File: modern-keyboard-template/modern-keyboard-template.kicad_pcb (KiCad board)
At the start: 2 copper layers, 44 x 44.1 mm, 25 parts, among them J1 USB_C_Receptacle_USB2.0, J2 Conn_01x05, U1 STM32F072CBT6, U2 PRTR5V0U2X, U3 XC6206PxxxMR-Regulator_Linear, U5 TXB0101

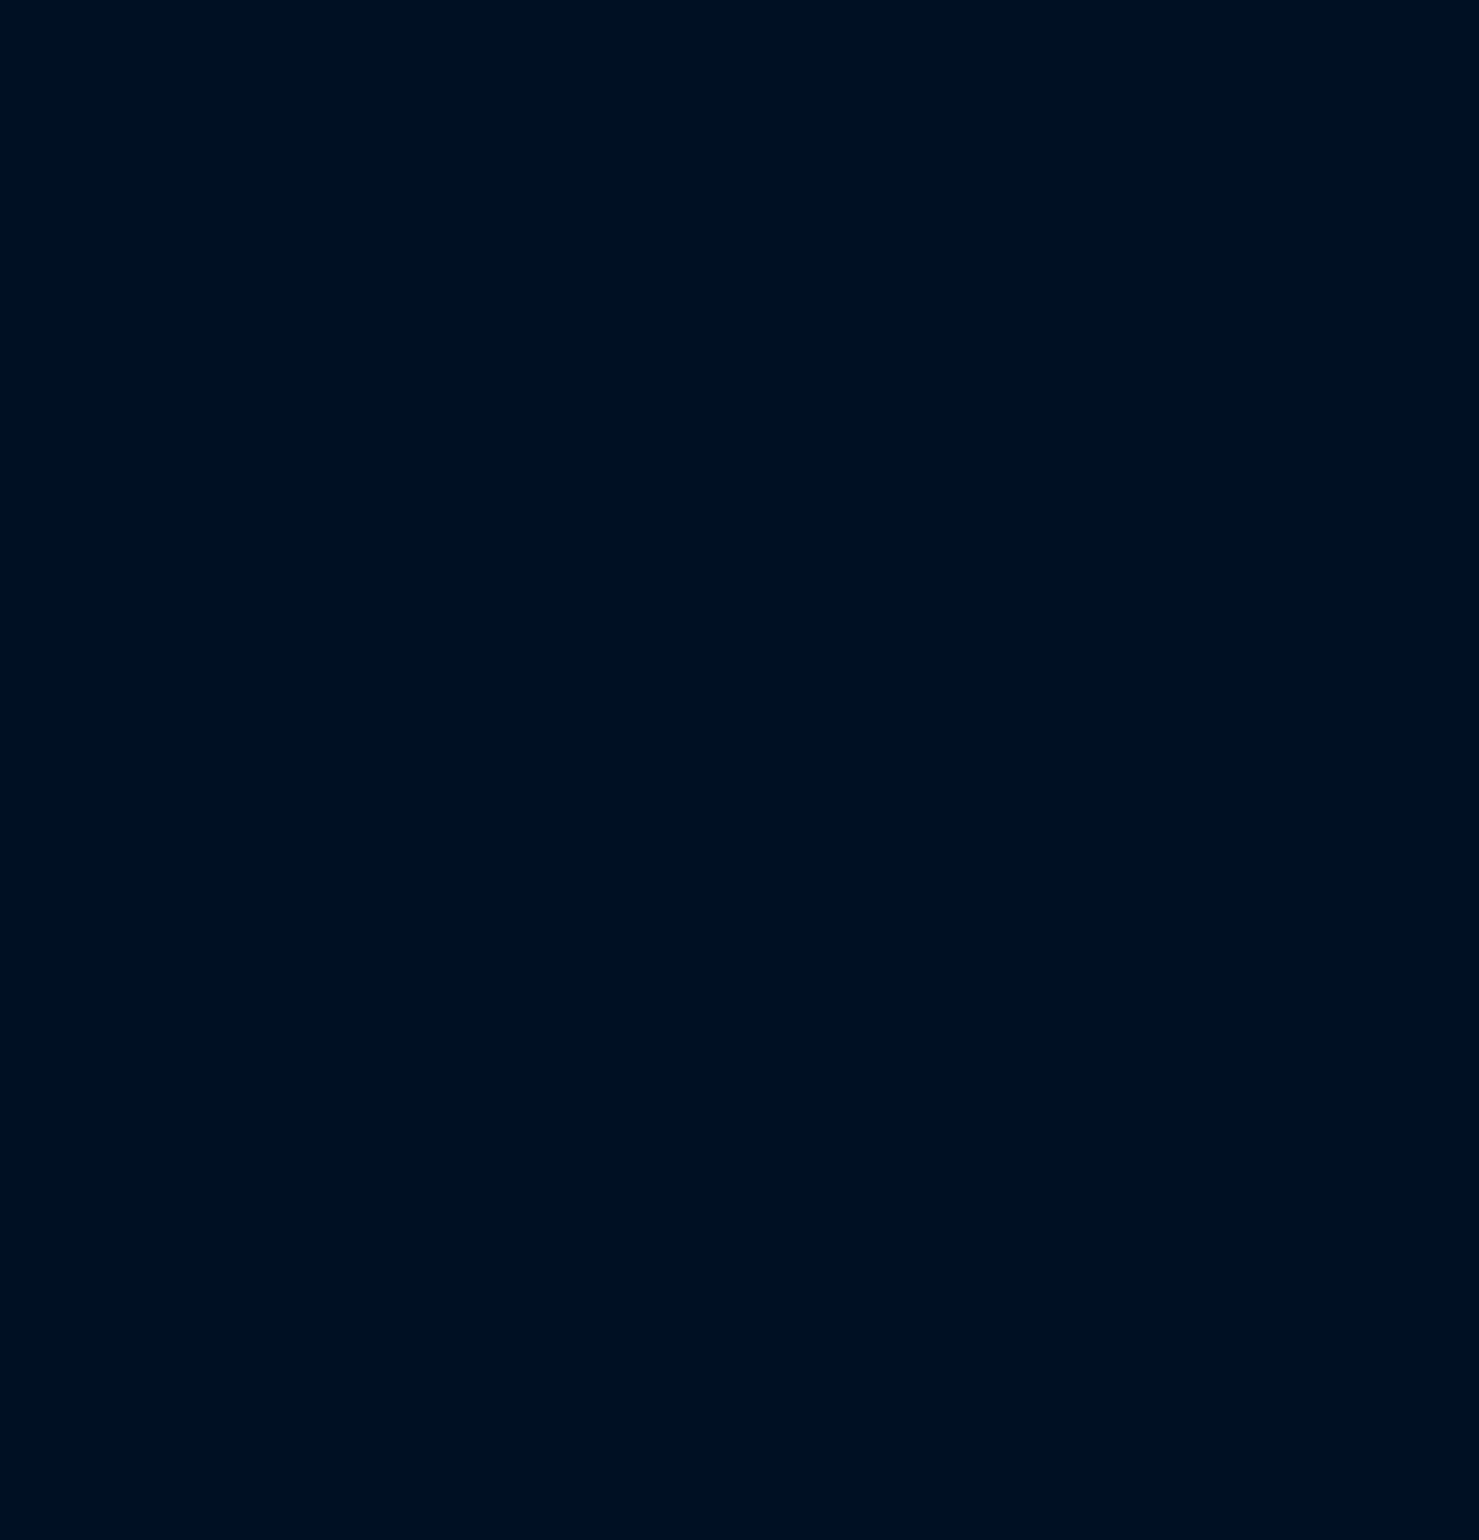
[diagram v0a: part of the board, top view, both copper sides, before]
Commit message: updated pcb w/ switches
need to revisit this entire design tbh
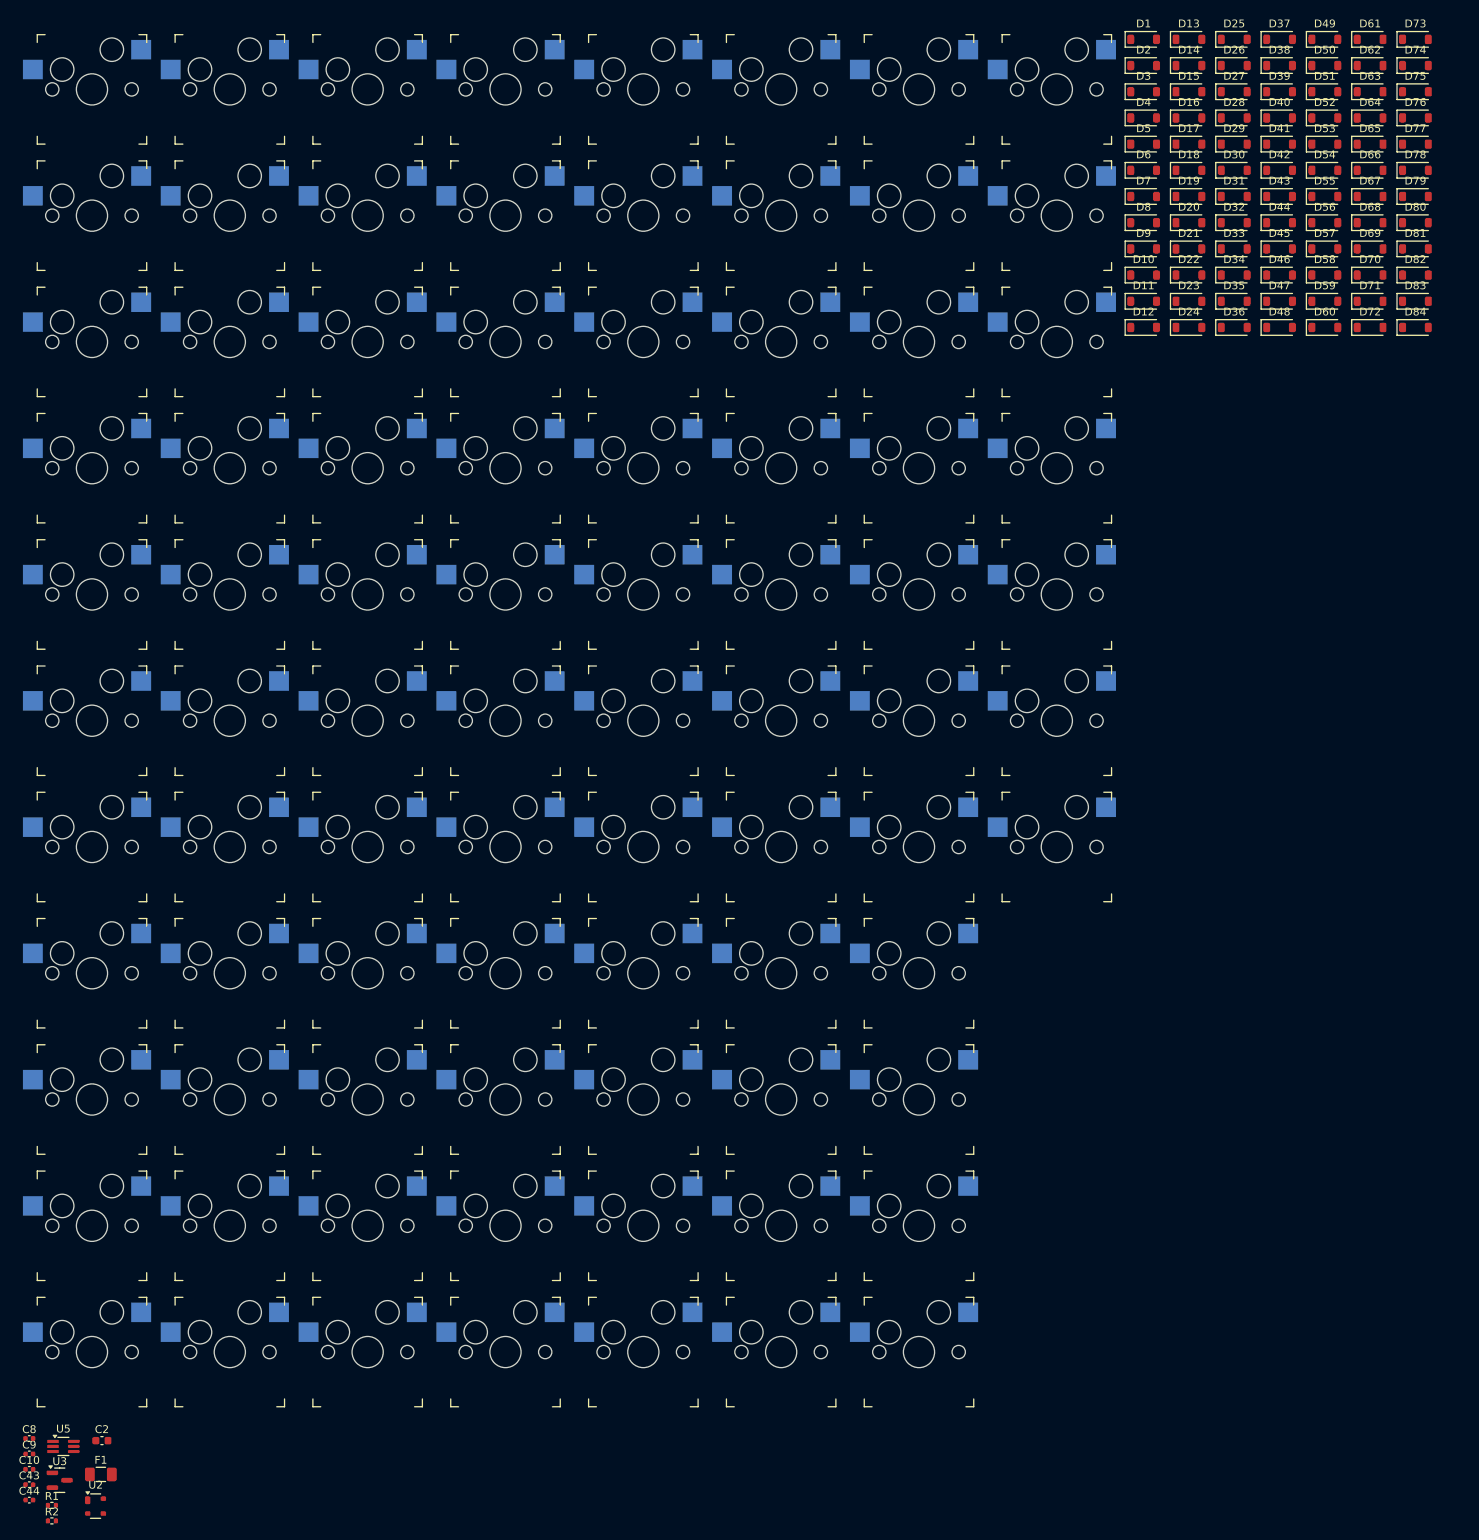
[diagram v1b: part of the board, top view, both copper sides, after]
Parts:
- added C10: 1uF, Capacitor_SMD:C_0402_1005Metric, F.Cu at (-32.3, 108.8)
- added C2: 10uF, Capacitor_SMD:C_0603_1608Metric, F.Cu at (-23.0, 105.2)
- added C43: 0.1uF, Capacitor_SMD:C_0402_1005Metric, F.Cu at (-32.3, 110.8)
- added C44: 0.1uF, Capacitor_SMD:C_0402_1005Metric, F.Cu at (-32.3, 112.8)
- added C8: 100nF, Capacitor_SMD:C_0402_1005Metric, F.Cu at (-32.3, 104.9)
- added C9: 1uF, Capacitor_SMD:C_0402_1005Metric, F.Cu at (-32.3, 106.9)
- added D1: D, Diode_SMD:D_SOD-123, F.Cu at (110.3, -74.1)
- added D10: D, Diode_SMD:D_SOD-123, F.Cu at (110.3, -43.9)
- added D11: D, Diode_SMD:D_SOD-123, F.Cu at (110.3, -40.6)
- added D12: D, Diode_SMD:D_SOD-123, F.Cu at (110.3, -37.2)
- added D13: D, Diode_SMD:D_SOD-123, F.Cu at (116.1, -74.1)
- added D14: D, Diode_SMD:D_SOD-123, F.Cu at (116.1, -70.7)
- added D15: D, Diode_SMD:D_SOD-123, F.Cu at (116.1, -67.4)
- added D16: D, Diode_SMD:D_SOD-123, F.Cu at (116.1, -64.0)
- added D17: D, Diode_SMD:D_SOD-123, F.Cu at (116.1, -60.7)
- added D18: D, Diode_SMD:D_SOD-123, F.Cu at (116.1, -57.3)
- added D19: D, Diode_SMD:D_SOD-123, F.Cu at (116.1, -54.0)
- added D2: D, Diode_SMD:D_SOD-123, F.Cu at (110.3, -70.7)
- added D20: D, Diode_SMD:D_SOD-123, F.Cu at (116.1, -50.6)
- added D21: D, Diode_SMD:D_SOD-123, F.Cu at (116.1, -47.3)
- added D22: D, Diode_SMD:D_SOD-123, F.Cu at (116.1, -43.9)
- added D23: D, Diode_SMD:D_SOD-123, F.Cu at (116.1, -40.6)
- added D24: D, Diode_SMD:D_SOD-123, F.Cu at (116.1, -37.2)
- added D25: D, Diode_SMD:D_SOD-123, F.Cu at (121.9, -74.1)
- added D26: D, Diode_SMD:D_SOD-123, F.Cu at (121.9, -70.7)
- added D27: D, Diode_SMD:D_SOD-123, F.Cu at (121.9, -67.4)
- added D28: D, Diode_SMD:D_SOD-123, F.Cu at (121.9, -64.0)
- added D29: D, Diode_SMD:D_SOD-123, F.Cu at (121.9, -60.7)
- added D3: D, Diode_SMD:D_SOD-123, F.Cu at (110.3, -67.4)
- added D30: D, Diode_SMD:D_SOD-123, F.Cu at (121.9, -57.3)
- added D31: D, Diode_SMD:D_SOD-123, F.Cu at (121.9, -54.0)
- added D32: D, Diode_SMD:D_SOD-123, F.Cu at (121.9, -50.6)
- added D33: D, Diode_SMD:D_SOD-123, F.Cu at (121.9, -47.3)
- added D34: D, Diode_SMD:D_SOD-123, F.Cu at (121.9, -43.9)
- added D35: D, Diode_SMD:D_SOD-123, F.Cu at (121.9, -40.6)
- added D36: D, Diode_SMD:D_SOD-123, F.Cu at (121.9, -37.2)
- added D37: D, Diode_SMD:D_SOD-123, F.Cu at (127.7, -74.1)
- added D38: D, Diode_SMD:D_SOD-123, F.Cu at (127.7, -70.7)
- added D39: D, Diode_SMD:D_SOD-123, F.Cu at (127.7, -67.4)
- added D4: D, Diode_SMD:D_SOD-123, F.Cu at (110.3, -64.0)
- added D40: D, Diode_SMD:D_SOD-123, F.Cu at (127.7, -64.0)
- added D41: D, Diode_SMD:D_SOD-123, F.Cu at (127.7, -60.7)
- added D42: D, Diode_SMD:D_SOD-123, F.Cu at (127.7, -57.3)
- added D43: D, Diode_SMD:D_SOD-123, F.Cu at (127.7, -54.0)
- added D44: D, Diode_SMD:D_SOD-123, F.Cu at (127.7, -50.6)
- added D45: D, Diode_SMD:D_SOD-123, F.Cu at (127.7, -47.3)
- added D46: D, Diode_SMD:D_SOD-123, F.Cu at (127.7, -43.9)
- added D47: D, Diode_SMD:D_SOD-123, F.Cu at (127.7, -40.6)
- added D48: D, Diode_SMD:D_SOD-123, F.Cu at (127.7, -37.2)
- added D49: D, Diode_SMD:D_SOD-123, F.Cu at (133.4, -74.1)
- added D5: D, Diode_SMD:D_SOD-123, F.Cu at (110.3, -60.7)
- added D50: D, Diode_SMD:D_SOD-123, F.Cu at (133.4, -70.7)
- added D51: D, Diode_SMD:D_SOD-123, F.Cu at (133.4, -67.4)
- added D52: D, Diode_SMD:D_SOD-123, F.Cu at (133.4, -64.0)
- added D53: D, Diode_SMD:D_SOD-123, F.Cu at (133.4, -60.7)
- added D54: D, Diode_SMD:D_SOD-123, F.Cu at (133.4, -57.3)
- added D55: D, Diode_SMD:D_SOD-123, F.Cu at (133.4, -54.0)
- added D56: D, Diode_SMD:D_SOD-123, F.Cu at (133.4, -50.6)
- added D57: D, Diode_SMD:D_SOD-123, F.Cu at (133.4, -47.3)
- added D58: D, Diode_SMD:D_SOD-123, F.Cu at (133.4, -43.9)
- added D59: D, Diode_SMD:D_SOD-123, F.Cu at (133.4, -40.6)
- added D6: D, Diode_SMD:D_SOD-123, F.Cu at (110.3, -57.3)
- added D60: D, Diode_SMD:D_SOD-123, F.Cu at (133.4, -37.2)
- added D61: D, Diode_SMD:D_SOD-123, F.Cu at (139.2, -74.1)
- added D62: D, Diode_SMD:D_SOD-123, F.Cu at (139.2, -70.7)
- added D63: D, Diode_SMD:D_SOD-123, F.Cu at (139.2, -67.4)
- added D64: D, Diode_SMD:D_SOD-123, F.Cu at (139.2, -64.0)
- added D65: D, Diode_SMD:D_SOD-123, F.Cu at (139.2, -60.7)
- added D66: D, Diode_SMD:D_SOD-123, F.Cu at (139.2, -57.3)
- added D67: D, Diode_SMD:D_SOD-123, F.Cu at (139.2, -54.0)
- added D68: D, Diode_SMD:D_SOD-123, F.Cu at (139.2, -50.6)
- added D69: D, Diode_SMD:D_SOD-123, F.Cu at (139.2, -47.3)
- added D7: D, Diode_SMD:D_SOD-123, F.Cu at (110.3, -54.0)
- added D70: D, Diode_SMD:D_SOD-123, F.Cu at (139.2, -43.9)
- added D71: D, Diode_SMD:D_SOD-123, F.Cu at (139.2, -40.6)
- added D72: D, Diode_SMD:D_SOD-123, F.Cu at (139.2, -37.2)
- added D73: D, Diode_SMD:D_SOD-123, F.Cu at (145.0, -74.1)
- added D74: D, Diode_SMD:D_SOD-123, F.Cu at (145.0, -70.7)
- added D75: D, Diode_SMD:D_SOD-123, F.Cu at (145.0, -67.4)
- added D76: D, Diode_SMD:D_SOD-123, F.Cu at (145.0, -64.0)
- added D77: D, Diode_SMD:D_SOD-123, F.Cu at (145.0, -60.7)
- added D78: D, Diode_SMD:D_SOD-123, F.Cu at (145.0, -57.3)
- added D79: D, Diode_SMD:D_SOD-123, F.Cu at (145.0, -54.0)
- added D8: D, Diode_SMD:D_SOD-123, F.Cu at (110.3, -50.6)
- added D80: D, Diode_SMD:D_SOD-123, F.Cu at (145.0, -50.6)
- added D81: D, Diode_SMD:D_SOD-123, F.Cu at (145.0, -47.3)
- added D82: D, Diode_SMD:D_SOD-123, F.Cu at (145.0, -43.9)
- added D83: D, Diode_SMD:D_SOD-123, F.Cu at (145.0, -40.6)
- added D84: D, Diode_SMD:D_SOD-123, F.Cu at (145.0, -37.2)
- added D9: D, Diode_SMD:D_SOD-123, F.Cu at (110.3, -47.3)
- added F1: 500mA, Fuse:Fuse_1206_3216Metric, F.Cu at (-23.1, 109.5)
- added R1: 5.1k, Resistor_SMD:R_0402_1005Metric, F.Cu at (-29.4, 113.4)
- added R2: 5.1k, Resistor_SMD:R_0402_1005Metric, F.Cu at (-29.4, 115.4)
- added SW1: ~, switches:Kailh_socket_MX, F.Cu at (-24.2, -67.7)
- added SW10: ~, switches:Kailh_socket_MX, F.Cu at (-24.2, 77.7)
- added SW11: ~, switches:Kailh_socket_MX, F.Cu at (-24.2, 93.8)
- added SW12: ~, switches:Kailh_socket_MX, F.Cu at (-6.62, -67.7)
- added SW13: ~, switches:Kailh_socket_MX, F.Cu at (-6.62, -51.5)
- added SW14: ~, switches:Kailh_socket_MX, F.Cu at (-6.62, -35.4)
- added SW15: ~, switches:Kailh_socket_MX, F.Cu at (-6.62, -19.2)
- added SW16: ~, switches:Kailh_socket_MX, F.Cu at (-6.62, -3.06)
- added SW17: ~, switches:Kailh_socket_MX, F.Cu at (-6.62, 13.1)
- added SW18: ~, switches:Kailh_socket_MX, F.Cu at (-6.62, 29.2)
- added SW19: ~, switches:Kailh_socket_MX, F.Cu at (-6.62, 45.4)
- added SW2: ~, switches:Kailh_socket_MX, F.Cu at (-24.2, -51.5)
- added SW20: ~, switches:Kailh_socket_MX, F.Cu at (-6.62, 61.5)
- added SW21: ~, switches:Kailh_socket_MX, F.Cu at (-6.62, 77.7)
- added SW22: ~, switches:Kailh_socket_MX, F.Cu at (-6.62, 93.8)
- added SW23: ~, switches:Kailh_socket_MX, F.Cu at (11.0, -67.7)
- added SW24: ~, switches:Kailh_socket_MX, F.Cu at (11.0, -51.5)
- added SW25: ~, switches:Kailh_socket_MX, F.Cu at (11.0, -35.4)
- added SW26: ~, switches:Kailh_socket_MX, F.Cu at (11.0, -19.2)
- added SW27: ~, switches:Kailh_socket_MX, F.Cu at (11.0, -3.06)
- added SW28: ~, switches:Kailh_socket_MX, F.Cu at (11.0, 13.1)
- added SW29: ~, switches:Kailh_socket_MX, F.Cu at (11.0, 29.2)
- added SW3: ~, switches:Kailh_socket_MX, F.Cu at (-24.2, -35.4)
- added SW30: ~, switches:Kailh_socket_MX, F.Cu at (11.0, 45.4)
- added SW31: ~, switches:Kailh_socket_MX, F.Cu at (11.0, 61.5)
- added SW32: ~, switches:Kailh_socket_MX, F.Cu at (11.0, 77.7)
- added SW33: ~, switches:Kailh_socket_MX, F.Cu at (11.0, 93.8)
- added SW34: ~, switches:Kailh_socket_MX, F.Cu at (28.6, -67.7)
- added SW35: ~, switches:Kailh_socket_MX, F.Cu at (28.6, -51.5)
- added SW36: ~, switches:Kailh_socket_MX, F.Cu at (28.6, -35.4)
- added SW37: ~, switches:Kailh_socket_MX, F.Cu at (28.6, -19.2)
- added SW38: ~, switches:Kailh_socket_MX, F.Cu at (28.6, -3.06)
- added SW39: ~, switches:Kailh_socket_MX, F.Cu at (28.6, 13.1)
- added SW4: ~, switches:Kailh_socket_MX, F.Cu at (-24.2, -19.2)
- added SW40: ~, switches:Kailh_socket_MX, F.Cu at (28.6, 29.2)
- added SW41: ~, switches:Kailh_socket_MX, F.Cu at (28.6, 45.4)
- added SW42: ~, switches:Kailh_socket_MX, F.Cu at (28.6, 61.5)
- added SW43: ~, switches:Kailh_socket_MX, F.Cu at (28.6, 77.7)
- added SW44: ~, switches:Kailh_socket_MX, F.Cu at (28.6, 93.8)
- added SW45: ~, switches:Kailh_socket_MX, F.Cu at (46.3, -67.7)
- added SW46: ~, switches:Kailh_socket_MX, F.Cu at (46.3, -51.5)
- added SW47: ~, switches:Kailh_socket_MX, F.Cu at (46.3, -35.4)
- added SW48: ~, switches:Kailh_socket_MX, F.Cu at (46.3, -19.2)
- added SW49: ~, switches:Kailh_socket_MX, F.Cu at (46.3, -3.06)
- added SW5: ~, switches:Kailh_socket_MX, F.Cu at (-24.2, -3.06)
- added SW50: ~, switches:Kailh_socket_MX, F.Cu at (46.3, 13.1)
- added SW51: ~, switches:Kailh_socket_MX, F.Cu at (46.3, 29.2)
- added SW52: ~, switches:Kailh_socket_MX, F.Cu at (46.3, 45.4)
- added SW53: ~, switches:Kailh_socket_MX, F.Cu at (46.3, 61.5)
- added SW54: ~, switches:Kailh_socket_MX, F.Cu at (46.3, 77.7)
- added SW55: ~, switches:Kailh_socket_MX, F.Cu at (46.3, 93.8)
- added SW56: ~, switches:Kailh_socket_MX, F.Cu at (63.9, -67.7)
- added SW57: ~, switches:Kailh_socket_MX, F.Cu at (63.9, -51.5)
- added SW58: ~, switches:Kailh_socket_MX, F.Cu at (63.9, -35.4)
- added SW59: ~, switches:Kailh_socket_MX, F.Cu at (63.9, -19.2)
- added SW6: ~, switches:Kailh_socket_MX, F.Cu at (-24.2, 13.1)
- added SW60: ~, switches:Kailh_socket_MX, F.Cu at (63.9, -3.06)
- added SW61: ~, switches:Kailh_socket_MX, F.Cu at (63.9, 13.1)
- added SW62: ~, switches:Kailh_socket_MX, F.Cu at (63.9, 29.2)
- added SW63: ~, switches:Kailh_socket_MX, F.Cu at (63.9, 45.4)
- added SW64: ~, switches:Kailh_socket_MX, F.Cu at (63.9, 61.5)
- added SW65: ~, switches:Kailh_socket_MX, F.Cu at (63.9, 77.7)
- added SW66: ~, switches:Kailh_socket_MX, F.Cu at (63.9, 93.8)
- added SW67: ~, switches:Kailh_socket_MX, F.Cu at (81.5, -67.7)
- added SW68: ~, switches:Kailh_socket_MX, F.Cu at (81.5, -51.5)
- added SW69: ~, switches:Kailh_socket_MX, F.Cu at (81.5, -35.4)
- added SW7: ~, switches:Kailh_socket_MX, F.Cu at (-24.2, 29.2)
- added SW70: ~, switches:Kailh_socket_MX, F.Cu at (81.5, -19.2)
- added SW71: ~, switches:Kailh_socket_MX, F.Cu at (81.5, -3.06)
- added SW72: ~, switches:Kailh_socket_MX, F.Cu at (81.5, 13.1)
- added SW73: ~, switches:Kailh_socket_MX, F.Cu at (81.5, 29.2)
- added SW74: ~, switches:Kailh_socket_MX, F.Cu at (81.5, 45.4)
- added SW75: ~, switches:Kailh_socket_MX, F.Cu at (81.5, 61.5)
- added SW76: ~, switches:Kailh_socket_MX, F.Cu at (81.5, 77.7)
- added SW77: ~, switches:Kailh_socket_MX, F.Cu at (81.5, 93.8)
- added SW78: ~, switches:Kailh_socket_MX, F.Cu at (99.2, -67.7)
- added SW79: ~, switches:Kailh_socket_MX, F.Cu at (99.2, -51.5)
- added SW8: ~, switches:Kailh_socket_MX, F.Cu at (-24.2, 45.4)
- added SW80: ~, switches:Kailh_socket_MX, F.Cu at (99.2, -35.4)
- added SW81: ~, switches:Kailh_socket_MX, F.Cu at (99.2, -19.2)
- added SW82: ~, switches:Kailh_socket_MX, F.Cu at (99.2, -3.06)
- added SW83: ~, switches:Kailh_socket_MX, F.Cu at (99.2, 13.1)
- added SW84: ~, switches:Kailh_socket_MX, F.Cu at (99.2, 29.2)
- added SW9: ~, switches:Kailh_socket_MX, F.Cu at (-24.2, 61.5)
- added U2: PRTR5V0U2X, Package_TO_SOT_SMD:SOT-143, F.Cu at (-23.8, 113.5)
- added U3: XC6206PxxxMR-Regulator_Linear, Package_TO_SOT_SMD:SOT-23, F.Cu at (-28.4, 110.2)
- added U5: TXB0101, Package_TO_SOT_SMD:SOT-363_SC-70-6_Handsoldering, F.Cu at (-27.9, 105.9)

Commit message: added layout file, router keys
added layout file in /dependencies
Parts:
- removed the C10 at (-32.3, 108.8)
- removed the C10 at (174.6, 51.2)
- removed the C2 at (-23.0, 105.2)
- removed the C2 at (174.7, 52.5)
- removed the C43 at (-32.3, 110.8)
- removed the C43 at (179.2, 40.2)
- removed the C44 at (-32.3, 112.8)
- removed the C44 at (176.2, 40.2)
- removed the C8 at (-32.3, 104.9)
- removed the C8 at (199.0, 50.4)
- removed the C9 at (-32.3, 106.9)
- removed the C9 at (172.0, 48.4)
- removed the F1 at (-23.1, 109.5)
- removed the F1 at (185.3, 41.6)
- removed the R1 at (-29.4, 113.4)
- removed the R1 at (200.5, 49.0)
- removed the R2 at (-29.4, 115.4)
- removed the R2 at (199.5, 47.7)
- removed the U2 at (-23.8, 113.5)
- removed the U2 at (196.5, 49.0)
- removed the U3 at (-28.4, 110.2)
- removed the U3 at (174.5, 48.9)
- removed the U5 at (-27.9, 105.9)
- removed the U5 at (177.7, 42.3)
- added C10: 1uF, Capacitor_SMD:C_0402_1005Metric, B.Cu at (352.8, 39.6)
- added C2: 10uF, Capacitor_SMD:C_0603_1608Metric, B.Cu at (352.9, 40.9)
- added C43: 0.1uF, Capacitor_SMD:C_0402_1005Metric, B.Cu at (357.4, 28.7)
- added C44: 0.1uF, Capacitor_SMD:C_0402_1005Metric, B.Cu at (354.4, 28.7)
- added C8: 100nF, Capacitor_SMD:C_0402_1005Metric, B.Cu at (377.2, 38.9)
- added C9: 1uF, Capacitor_SMD:C_0402_1005Metric, B.Cu at (350.2, 36.9)
- added F1: 500mA, Fuse:Fuse_1206_3216Metric, B.Cu at (363.5, 30.0)
- added R1: 5.1k, Resistor_SMD:R_0402_1005Metric, B.Cu at (378.7, 37.4)
- added R2: 5.1k, Resistor_SMD:R_0402_1005Metric, B.Cu at (377.7, 36.2)
- added U2: PRTR5V0U2X, Package_TO_SOT_SMD:SOT-143, B.Cu at (374.7, 37.4)
- added U3: XC6206PxxxMR-Regulator_Linear, Package_TO_SOT_SMD:SOT-23, B.Cu at (352.7, 37.4)
- added U5: TXB0101, Package_TO_SOT_SMD:SOT-363_SC-70-6_Handsoldering, B.Cu at (355.9, 30.7)
- D1, D72, D84: moved to B.Cu
- D10: renamed from D47; moved to B.Cu
- D11: renamed from D52; moved to B.Cu
- D12: renamed from D58; moved to B.Cu
- D13: renamed from D64; moved to B.Cu
- D14: renamed from D69; moved to B.Cu
- D15: renamed from D74; moved to B.Cu
- D16: renamed from D79; moved to B.Cu
- D17: renamed from D2; moved to B.Cu
- D18: renamed from D7; moved to B.Cu
- D19: renamed from D11; moved to B.Cu
- D2: renamed from D6; moved to B.Cu
- D20: renamed from D16; moved to B.Cu
- D21: renamed from D22; moved to B.Cu
- D22: renamed from D27; moved to B.Cu
- D23: renamed from D32; moved to B.Cu
- D24: renamed from D38; moved to B.Cu
- D25: renamed from D43; moved to B.Cu
- D26: renamed from D48; moved to B.Cu
- D27: renamed from D53; moved to B.Cu
- D28: renamed from D59; moved to B.Cu
- D29: renamed from D65; moved to B.Cu
- D3: renamed from D10; moved to B.Cu
- D30: renamed from D75; moved to B.Cu
- D31: renamed from D80; moved to B.Cu
- D32: renamed from D3; moved to B.Cu
- D33: renamed from D12; moved to B.Cu
- D34: renamed from D17; moved to B.Cu
- D35: renamed from D23; moved to B.Cu
- D36: renamed from D28; moved to B.Cu
- D37: renamed from D33; moved to B.Cu
- D38: renamed from D39; moved to B.Cu
- D39: renamed from D44; moved to B.Cu
- D4: renamed from D15; moved to B.Cu
- D40: renamed from D49; moved to B.Cu
- D41: renamed from D54; moved to B.Cu
- D42: renamed from D60; moved to B.Cu
- D43: renamed from D66; moved to B.Cu
- D44: renamed from D70; moved to B.Cu
- D45: renamed from D76; moved to B.Cu
- D46: renamed from D81; moved to B.Cu
- D47: renamed from D4; moved to B.Cu
- D48: renamed from D13; moved to B.Cu
- D49: renamed from D18; moved to B.Cu
- D5: renamed from D21; moved to B.Cu
- D50: renamed from D24; moved to B.Cu
- D51: renamed from D29; moved to B.Cu
- D52: renamed from D34; moved to B.Cu
- D53: renamed from D40; moved to B.Cu
- D54: renamed from D45; moved to B.Cu
- D55: renamed from D50; moved to B.Cu
- D56: renamed from D55; moved to B.Cu
- D57: renamed from D61; moved to B.Cu
- D58: renamed from D67; moved to B.Cu
- D59: renamed from D71; moved to B.Cu
- D6: renamed from D26; moved to B.Cu
- D60: renamed from D82; moved to B.Cu
- D61: renamed from D8; moved to B.Cu
- D62: renamed from D14; moved to B.Cu
- D63: renamed from D19; moved to B.Cu
- D64: renamed from D25; moved to B.Cu
- D65: renamed from D30; moved to B.Cu
- D66: renamed from D35; moved to B.Cu
- D67: renamed from D41; moved to B.Cu
- D68: renamed from D46; moved to B.Cu
- D69: renamed from D51; moved to B.Cu
- D7: renamed from D31; moved to B.Cu
- D70: renamed from D56; moved to B.Cu
- D71: renamed from D62; moved to B.Cu
- D73: renamed from D77; moved to B.Cu
- D74: renamed from D83; moved to B.Cu
- D75: renamed from D5; moved to B.Cu
- D76: renamed from D9; moved to B.Cu
- D77: renamed from D20; moved to B.Cu
- D78: renamed from D36; moved to B.Cu
- D79: renamed from D57; moved to B.Cu
- D8: renamed from D37; moved to B.Cu
- D80: renamed from D63; moved to B.Cu
- D81: renamed from D68; moved to B.Cu
- D82: renamed from D73; moved to B.Cu
- D83: renamed from D78; moved to B.Cu
- D9: renamed from D42; moved to B.Cu
- moved SW83 287.6 mm to (304.8, 133.3)
- moved SW81 261.6 mm to (266.7, 133.3)
- moved D82 256.2 mm to (290.8, 136.7), turned to 90 degrees
- moved D83 254.5 mm to (309.9, 136.7), turned to 90 degrees
- moved D84 253.1 mm to (328.9, 136.7), turned to 90 degrees
- moved SW70 248.6 mm to (233.4, 114.3)
- moved SW84 247.6 mm to (323.9, 133.3)
- moved SW79 247.6 mm to (228.6, 133.3)
- moved SW74 246.4 mm to (323.9, 114.3)
- moved SW60 245.3 mm to (323.9, 95.2)
- moved SW46 244.1 mm to (323.9, 76.2)
- moved SW58 243.1 mm to (261.9, 95.2)
- moved SW31 243.0 mm to (323.9, 57.1)
- moved D73 242.8 mm to (309.9, 117.6), turned to 90 degrees
- moved D74 242.6 mm to (328.9, 117.6), turned to 90 degrees
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- renumbered SW47 to SW10, SW52 to SW11, SW58 to SW12, SW64 to SW13, SW69 to SW14, SW74 to SW15, SW79 to SW16, SW2 to SW17, SW7 to SW18, SW11 to SW19, SW6 to SW2, SW16 to SW20, SW22 to SW21, SW27 to SW22, SW32 to SW23, SW38 to SW24, SW43 to SW25, SW48 to SW26, SW53 to SW27, SW59 to SW28, SW65 to SW29, SW10 to SW3, SW75 to SW30, SW80 to SW31, SW3 to SW32, SW12 to SW33, SW17 to SW34, SW23 to SW35, SW28 to SW36, SW33 to SW37, SW39 to SW38, SW44 to SW39, SW15 to SW4, SW49 to SW40, SW54 to SW41, SW60 to SW42, SW66 to SW43, SW70 to SW44, SW76 to SW45, SW81 to SW46, SW4 to SW47, SW13 to SW48, SW18 to SW49, SW21 to SW5, SW24 to SW50, SW29 to SW51, SW34 to SW52, SW40 to SW53, SW45 to SW54, SW50 to SW55, SW55 to SW56, SW61 to SW57, SW67 to SW58, SW71 to SW59, SW26 to SW6, SW82 to SW60, SW8 to SW61, SW14 to SW62, SW19 to SW63, SW25 to SW64, SW30 to SW65, SW35 to SW66, SW41 to SW67, SW46 to SW68, SW51 to SW69, SW31 to SW7, SW56 to SW70, SW62 to SW71, SW77 to SW73, SW83 to SW74, SW5 to SW75, SW9 to SW76, SW20 to SW77, SW36 to SW78, SW57 to SW79, SW37 to SW8, SW63 to SW80, SW68 to SW81, SW73 to SW82, SW78 to SW83, SW42 to SW9
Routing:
- net row0: track 0.00 -> 285.9 mm, vias 0 -> 16
- net row1: track 0.00 -> 285.9 mm, vias 0 -> 12
- net row5: track 0.00 -> 283.4 mm
- net row2: track 0.00 -> 281.0 mm
- net row3: track 0.00 -> 278.6 mm
- net row4: track 0.00 -> 273.8 mm
- net col13: track 0.00 -> 115.0 mm, vias 0 -> 6
- net col1: track 0.00 -> 112.5 mm, vias 0 -> 6
- net col14: track 0.00 -> 110.9 mm, vias 0 -> 6
- net col3: track 0.00 -> 110.4 mm, vias 0 -> 6
- net col10: track 0.00 -> 107.3 mm, vias 0 -> 10
- net col11: track 0.00 -> 107.2 mm, vias 0 -> 10
- net col12: track 0.00 -> 106.4 mm, vias 0 -> 6
- net col6: track 0.00 -> 106.2 mm, vias 0 -> 6
- net col0: track 0.00 -> 100.2 mm
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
